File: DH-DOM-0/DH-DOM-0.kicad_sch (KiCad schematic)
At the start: 41 parts, among them J1 USB_C_Receptacle_USB2.0_14P, J2 Conn_01x02, Q1 FDN340P, SW1 RST, SW2 BOOT, U3 LSM6DSOXTR, U4 MMC5983MA, U5 NCP1117-3.3_SOT223, U6 TVS1400DRV, U7 ESP32-S3-WROOM-1-N16R8, U8 TP4057, U9 ST7789

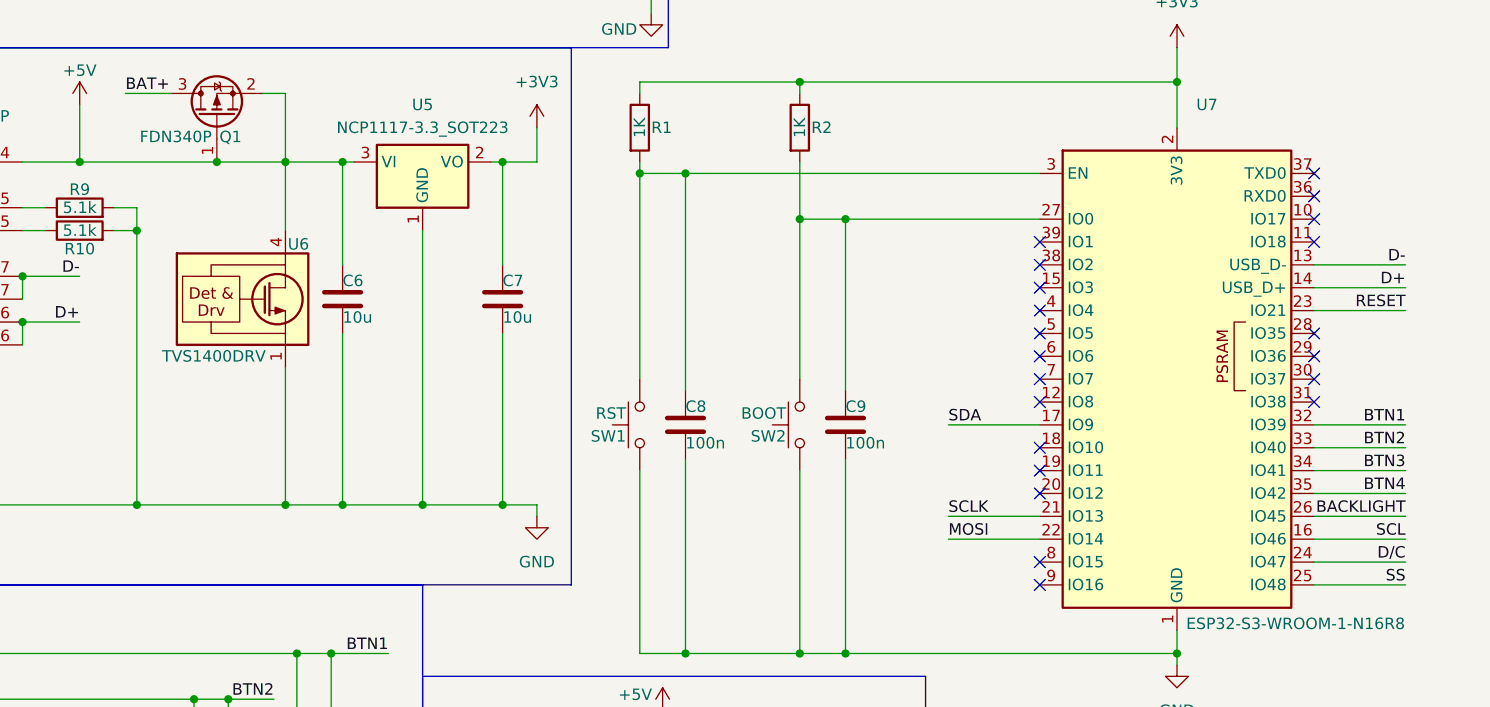
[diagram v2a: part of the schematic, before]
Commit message: fix
rerouted misrouted boot settings pins
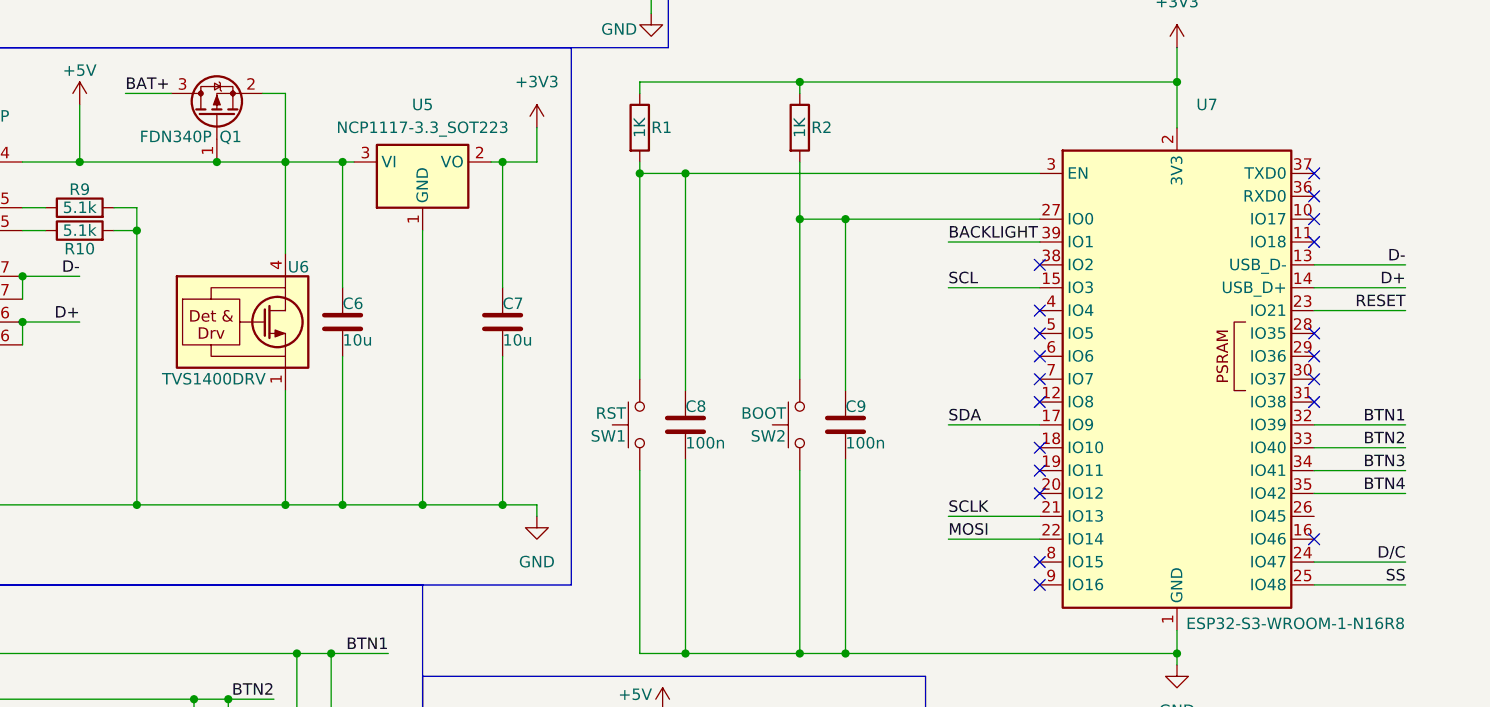
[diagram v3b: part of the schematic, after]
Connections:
- net BACKLIGHT: now also U7.39 (IO1); no longer U7.26 (IO45)
- net SCL: now also U7.15 (IO3); no longer U7.16 (IO46)
- no-connect marks 31 -> 30
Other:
- moved on the sheet: C6, C7, U6
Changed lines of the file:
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@@
 	)
 	(junction
+		(at 96.52 106.68)
+		(diameter 0)
+		(color 0 0 0 0)
+	)
+	(junction
 		(at 54.61 133.35)
 		(diameter 0)
@@
 	)
 	(junction
-		(at 96.52 106.68)
-		(diameter 0)
-		(color 0 0 0 0)
-	)
-	(junction
 		(at 134.62 123.19)
 		(diameter 0)
@@
 	)
 	(junction
-		(at 96.52 68.58)
-		(diameter 0)
-		(color 0 0 0 0)
-	)
-	(junction
 		(at 100.33 130.81)
 		(diameter 0)
@@
 	)
 	(junction
-		(at 78.74 68.58)
+		(at 96.52 68.58)
 		(diameter 0)
 		(color 0 0 0 0)
@@
 	)
 	(junction
+		(at 72.39 106.68)
+		(diameter 0)
+		(color 0 0 0 0)
+	)
+	(junction
 		(at 62.23 157.48)
 		(diameter 0)
@@
 	)
 	(junction
-		(at 73.66 157.48)
+		(at 78.74 68.58)
 		(diameter 0)
 		(color 0 0 0 0)
 	)
 	(junction
-		(at 111.76 69.85)
+		(at 73.66 157.48)
 		(diameter 0)
 		(color 0 0 0 0)
 	)
 	(junction
-		(at 78.74 106.68)
+		(at 111.76 69.85)
 		(diameter 0)
 		(color 0 0 0 0)
@@
 	)
 	(junction
-		(at 72.39 106.68)
-		(diameter 0)
-		(color 0 0 0 0)
-	)
-	(junction
 		(at 15.24 128.27)
 		(diameter 0)
@@
 	)
 	(junction
+		(at 78.74 106.68)
+		(diameter 0)
+		(color 0 0 0 0)
+	)
+	(junction
 		(at 73.66 123.19)
 		(diameter 0)
@@
 	)
 	(no_connect
-		(at 156.21 82.55)
-	)
-	(no_connect
-		(at 156.21 113.03)
-	)
-	(no_connect
 		(at 186.69 92.71)
 	)
@@
 	)
 	(no_connect
+		(at 156.21 113.03)
+	)
+	(no_connect
 		(at 90.17 38.1)
 	)
@@
 	)
 	(no_connect
-		(at 156.21 77.47)
-	)
-	(no_connect
 		(at 156.21 90.17)
 	)
@@
 	)
 	(no_connect
+		(at 186.69 110.49)
+	)
+	(no_connect
 		(at 156.21 100.33)
 	)
@@
 	(wire
 		(pts
+			(xy 146.05 77.47) (xy 156.21 77.47)
+		)
+		(stroke
+			(width 0)
+			(type default)
+		)
+	)
+	(wire
+		(pts
 			(xy 43.18 73.66) (xy 45.72 73.66)
 		)
@@
 	(wire
 		(pts
-			(xy 72.39 91.44) (xy 72.39 106.68)
+			(xy 72.39 93.98) (xy 72.39 106.68)
 		)
 		(stroke
@@
 	(wire
 		(pts
-			(xy 186.69 110.49) (xy 196.85 110.49)
-		)
-		(stroke
-			(width 0)
-			(type default)
-		)
-	)
-	(wire
-		(pts
 			(xy 15.24 38.1) (xy 25.4 38.1)
 		)
@@
 	(wire
 		(pts
-			(xy 96.52 87.63) (xy 96.52 106.68)
+			(xy 96.52 90.17) (xy 96.52 106.68)
 		)
 		(stroke
@@
 	(wire
 		(pts
-			(xy 96.52 68.58) (xy 96.52 80.01)
+			(xy 96.52 68.58) (xy 96.52 82.55)
 		)
 		(stroke
@@
 	(wire
 		(pts
-			(xy 78.74 80.01) (xy 78.74 68.58)
+			(xy 78.74 82.55) (xy 78.74 68.58)
 		)
 		(stroke
@@
 	(wire
 		(pts
-			(xy 186.69 107.95) (xy 196.85 107.95)
+			(xy 146.05 82.55) (xy 156.21 82.55)
 		)
 		(stroke
@@
 	(wire
 		(pts
-			(xy 78.74 87.63) (xy 78.74 106.68)
+			(xy 78.74 90.17) (xy 78.74 106.68)
 		)
 		(stroke
@@
 	(wire
 		(pts
-			(xy 72.39 68.58) (xy 72.39 76.2)
+			(xy 72.39 68.58) (xy 72.39 78.74)
 		)
 		(stroke
@@
 	)
 	(label "BACKLIGHT"
-		(at 196.85 107.95 180)
+		(at 146.05 77.47 0)
 		(effects
 			(font
 				(size 1.27 1.27)
 			)
-			(justify right bottom)
+			(justify left bottom)
 		)
 	)
@@
 	)
 	(label "SCL"
-		(at 196.85 110.49 180)
+		(at 146.05 82.55 0)
 		(effects
 			(font
 				(size 1.27 1.27)
 			)
-			(justify right bottom)
+			(justify left bottom)
 		)
 	)
@@
 	(symbol
 		(lib_id "Power_Protection:TVS1400DRV")
-		(at 72.39 83.82 0)
+		(at 72.39 86.36 0)
 		(unit 1)
 		(body_style 1)
@@
 		(dnp no)
 		(property "Reference" "U6"
-			(at 72.644 77.724 0)
+			(at 72.644 80.264 0)
 			(show_name no)
 			(do_not_autoplace no)
@@
 		)
 		(property "Value" "TVS1400DRV"
-			(at 58.674 90.17 0)
+			(at 58.674 92.71 0)
 			(show_name no)
 			(do_not_autoplace no)
@@
 		)
 		(property "Footprint" "Package_SON:WSON-6-1EP_2x2mm_P0.65mm_EP1x1.6mm"
-			(at 77.47 92.71 0)
+			(at 77.47 95.25 0)
 			(hide yes)
 			(show_name no)
@@
 		)
 		(property "Datasheet" "http://www.ti.com/lit/ds/symlink/tvs1400.pdf"
-			(at 69.85 83.82 0)
+			(at 69.85 86.36 0)
 			(hide yes)
 			(show_name no)
@@
 		)
 		(property "Description" "Flat-Clamp Surge Protection Device. 14Vrwm, WSON-6"
-			(at 72.39 83.82 0)
+			(at 72.39 86.36 0)
 			(hide yes)
 			(show_name no)
@@
 	(symbol
 		(lib_id "Device:C")
-		(at 78.74 83.82 0)
+		(at 78.74 86.36 0)
 		(unit 1)
 		(body_style 1)
@@
 		(dnp no)
 		(property "Reference" "C6"
-			(at 78.74 81.788 0)
+			(at 78.74 84.328 0)
 			(show_name no)
 			(do_not_autoplace no)
@@
 		)
 		(property "Value" "10u"
-			(at 78.74 85.852 0)
+			(at 78.74 88.392 0)
 			(show_name no)
 			(do_not_autoplace no)
@@
 		)
 		(property "Footprint" "Capacitor_SMD:C_0805_2012Metric"
-			(at 79.7052 87.63 0)
+			(at 79.7052 90.17 0)
 			(hide yes)
 			(show_name no)
@@
 		)
 		(property "Datasheet" ""
-			(at 78.74 83.82 0)
+			(at 78.74 86.36 0)
 			(hide yes)
 			(show_name no)
@@
 		)
 		(property "Description" "Unpolarized capacitor"
-			(at 78.74 83.82 0)
+			(at 78.74 86.36 0)
 			(hide yes)
 			(show_name no)
@@
 	(symbol
 		(lib_id "Device:C")
-		(at 96.52 83.82 0)
+		(at 96.52 86.36 0)
 		(unit 1)
 		(body_style 1)
@@
 		(dnp no)
 		(property "Reference" "C7"
-			(at 96.52 81.788 0)
+			(at 96.52 84.328 0)
 			(show_name no)
 			(do_not_autoplace no)
@@
 		)
 		(property "Value" "10u"
-			(at 96.52 85.852 0)
+			(at 96.52 88.392 0)
 			(show_name no)
 			(do_not_autoplace no)
@@
 		)
 		(property "Footprint" "Capacitor_SMD:C_0805_2012Metric"
-			(at 97.4852 87.63 0)
+			(at 97.4852 90.17 0)
 			(hide yes)
 			(show_name no)
@@
 		)
 		(property "Datasheet" ""
-			(at 96.52 83.82 0)
+			(at 96.52 86.36 0)
 			(hide yes)
 			(show_name no)
@@
 		)
 		(property "Description" "Unpolarized capacitor"
-			(at 96.52 83.82 0)
+			(at 96.52 86.36 0)
 			(hide yes)
 			(show_name no)

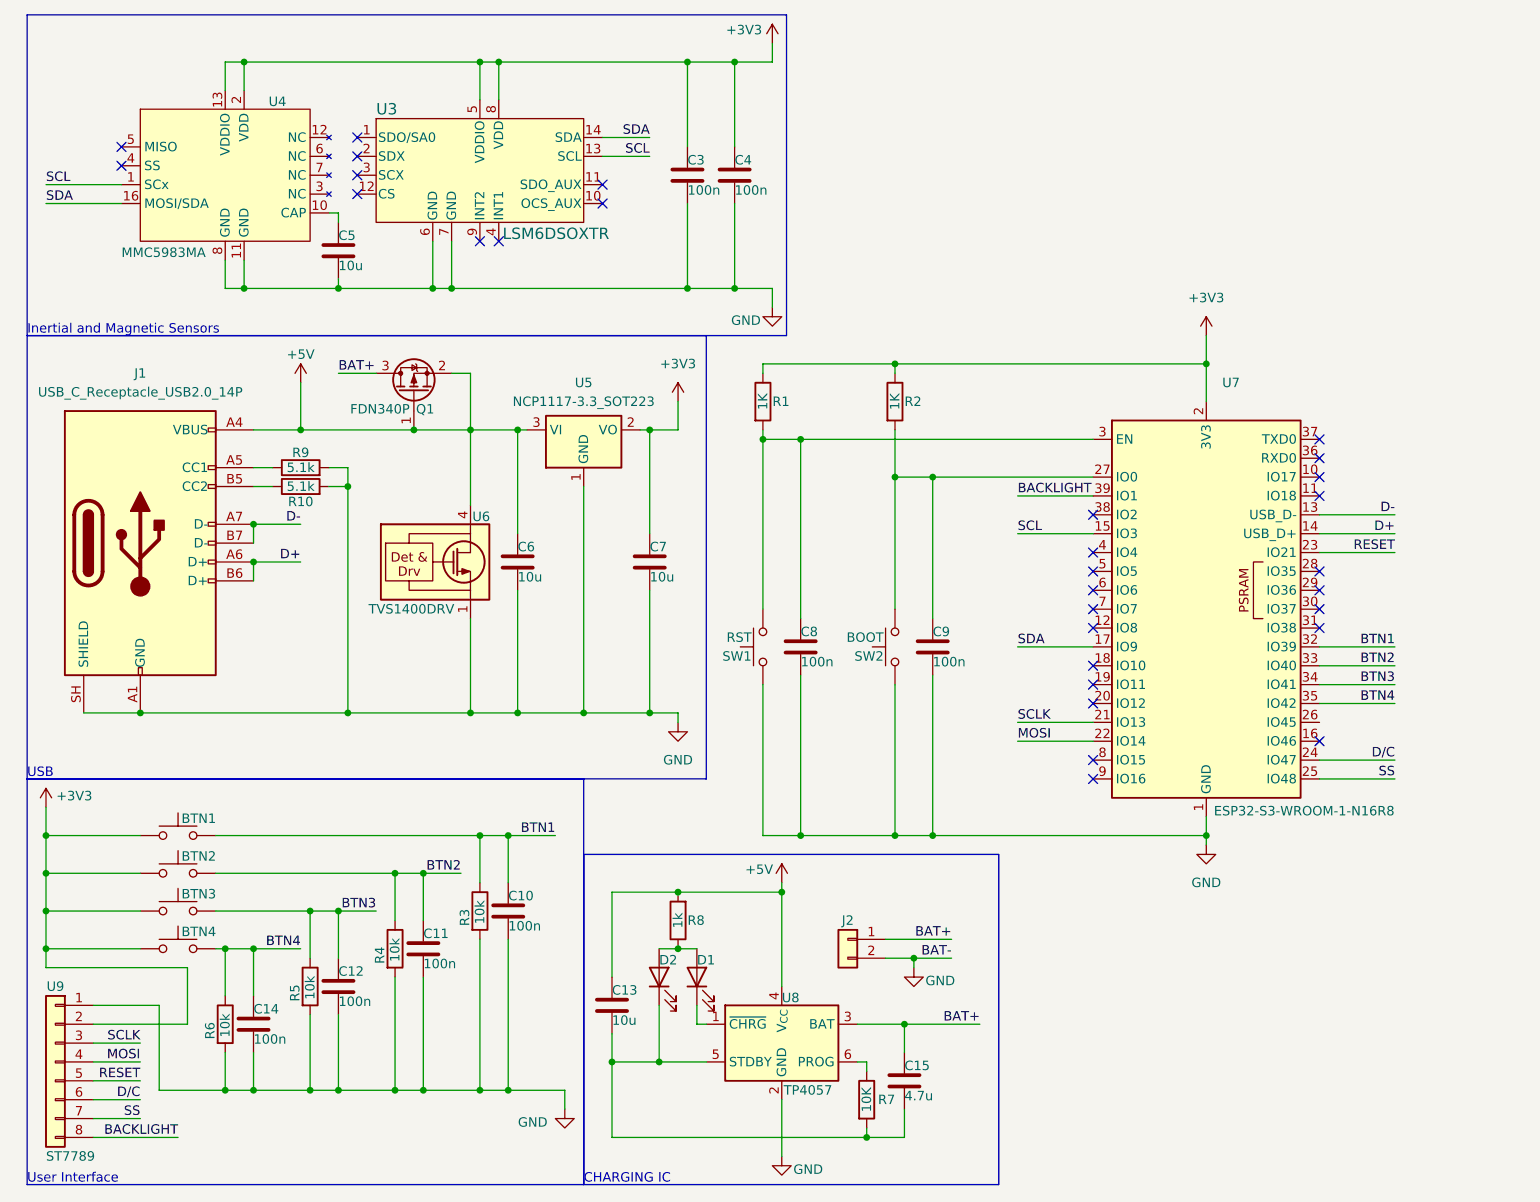
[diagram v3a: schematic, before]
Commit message: edit
added bmi270 backup just in case LSM6DSOXTR goes out of stock (only 2 left)
might switch to another imu idk, ESP32 I2C library is a must.

Currently building BOM
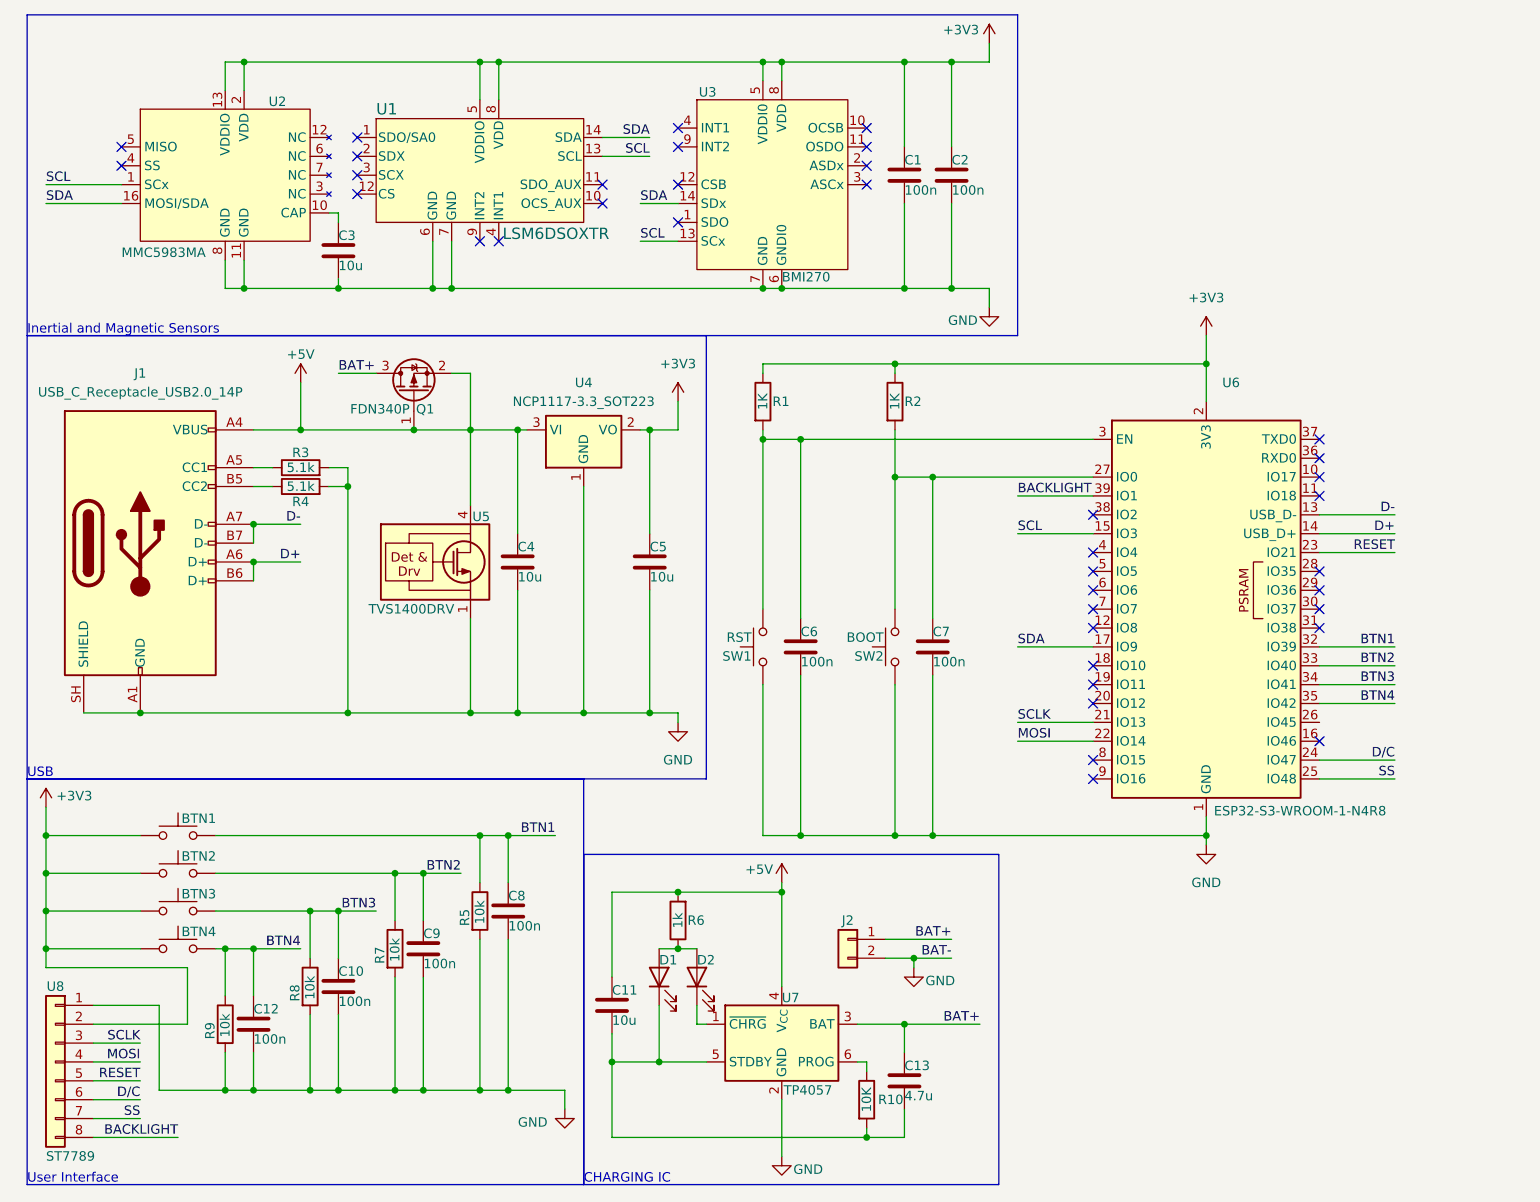
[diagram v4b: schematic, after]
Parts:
- added U3: BMI270, Package_LGA:Bosch_LGA-14_3x2.5mm_P0.5mm, symbol BMI270:BMI270
- U6: renamed from U7; value ESP32-S3-WROOM-1-N16R8 -> ESP32-S3-WROOM-1-N4R8
- renumbered C3 to C1, C12 to C10, C13 to C11, C14 to C12, C15 to C13, C4 to C2, C5 to C3, C6 to C4, C7 to C5, C8 to C6, C9 to C7, C10 to C8, C11 to C9, D2 to D1, D1 to D2, R7 to R10, R9 to R3, R10 to R4, R3 to R5, R8 to R6, R4 to R7, R5 to R8, R6 to R9, U3 to U1, U4 to U2, U5 to U4, U6 to U5, U8 to U7, U9 to U8
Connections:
- net +3V3: now also U3.5 (VDDI0), U3.8 (VDD)
- net GND: now also U3.6 (GNDI0), U3.7 (GND)
- net SCL: now also U3.13 (SCx)
- net SDA: now also U3.14 (SDx)
- no-connect marks 30 -> 38
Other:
- moved on the sheet: C1, C2

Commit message: edit
extra backup MEMS/IMU because digikey keeps running out
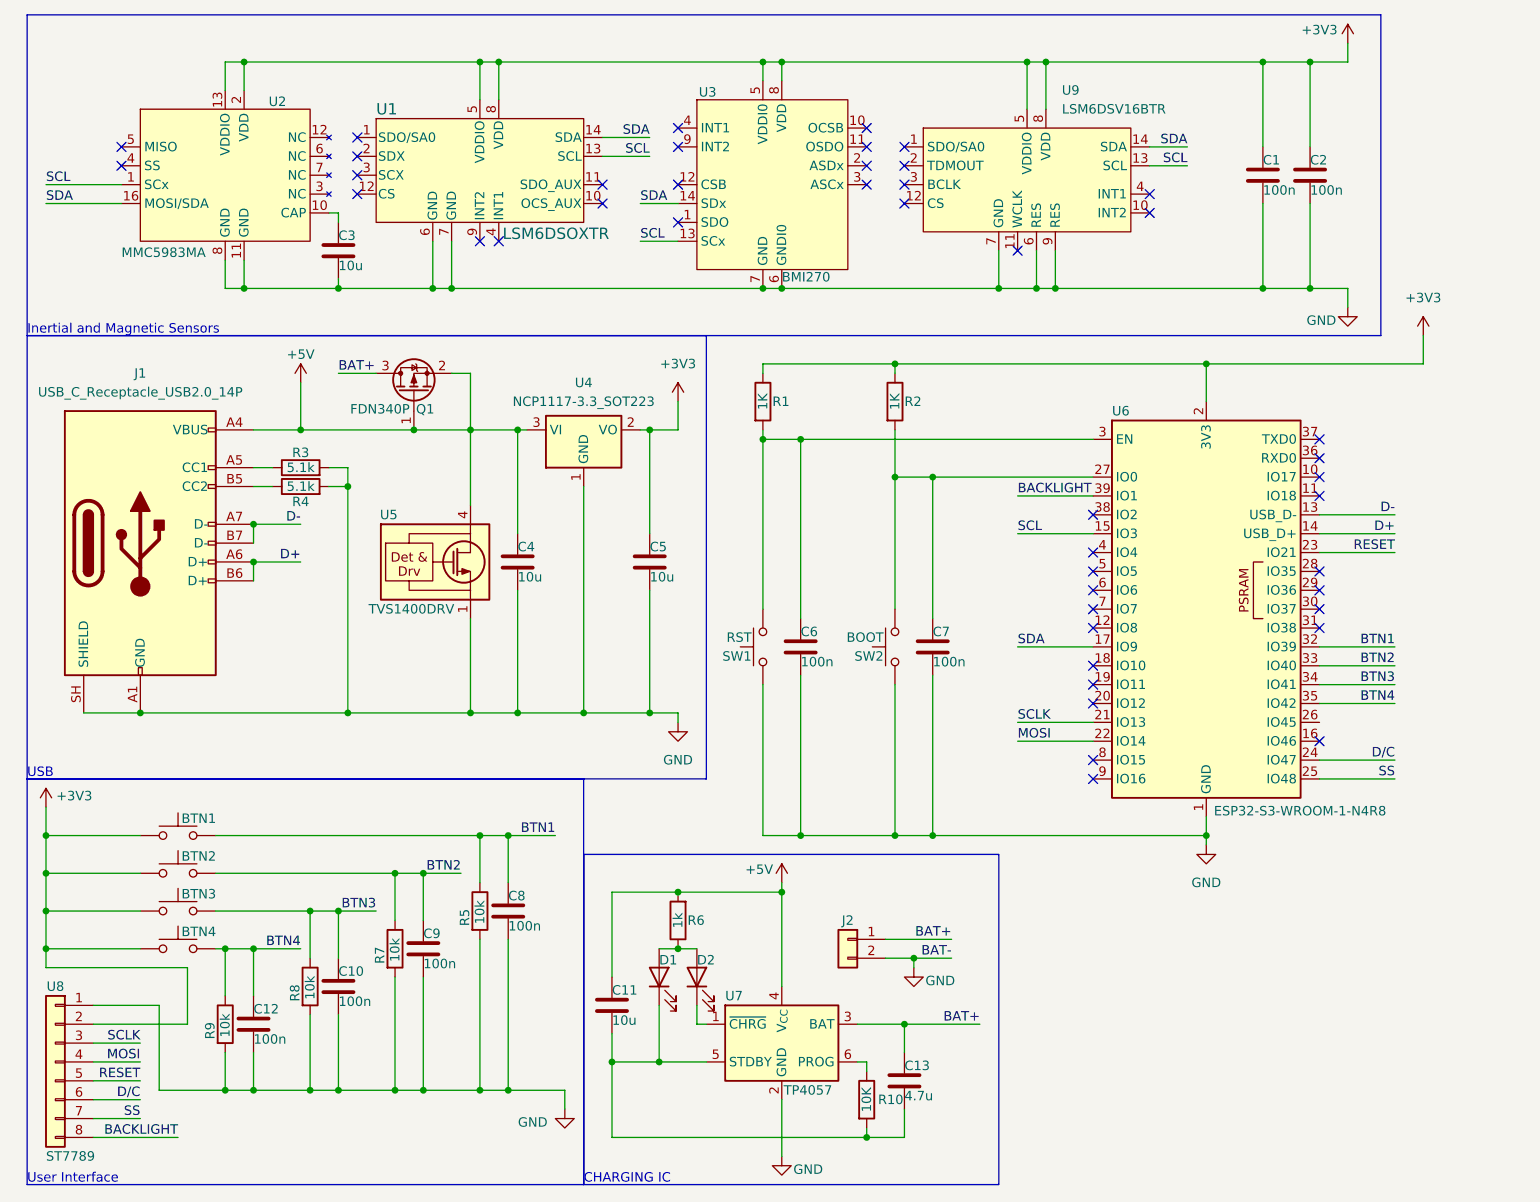
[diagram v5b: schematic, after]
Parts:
- added U9: LSM6DSV16BTR, Package_LGA:LGA-14_3x2.5mm_P0.5mm_LayoutBorder3x4y, symbol LSM6DSV16BTR:LSM6DSV16BTR
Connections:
- net +3V3: now also U9.5 (VDDIO), U9.8 (VDD)
- net GND: now also U9.6 (RES), U9.7 (GND), U9.9 (RES)
- net SCL: now also U9.13 (SCL)
- net SDA: now also U9.14 (SDA)
- no-connect marks 38 -> 45
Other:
- moved on the sheet: C1, C2
